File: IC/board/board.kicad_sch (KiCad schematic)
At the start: 35 parts, among them Q1 IRLZ44N, SW1 SW_Push, SW2 SW_Push, SW3 SW_Push, SW4 SW_Push, SW5 SW_Push, SW6 Rotary_Encoder_Switch, U1 L7805, U2 ATmega328P-PU, Y1 16Mhz

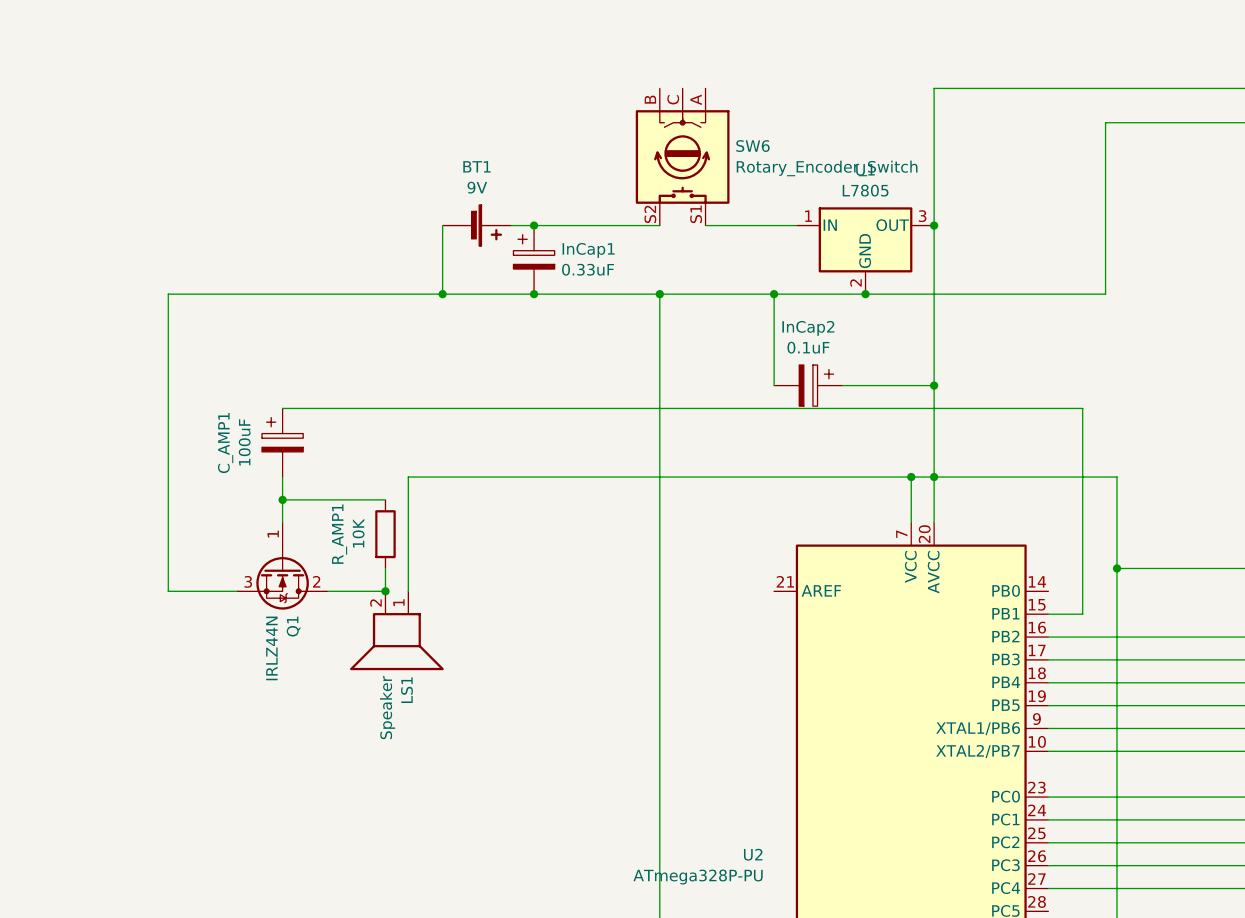
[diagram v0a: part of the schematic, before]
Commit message: Add PAM amplifier
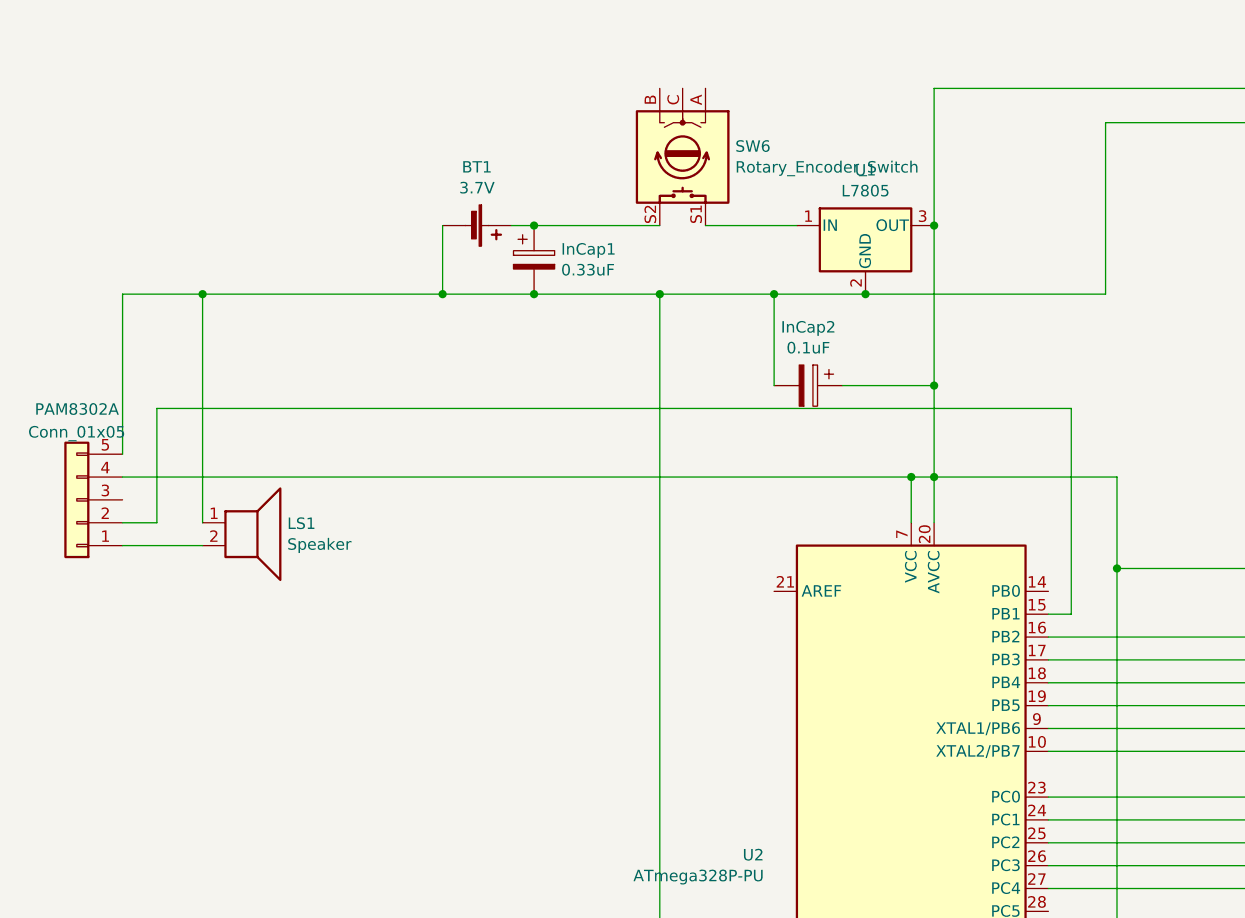
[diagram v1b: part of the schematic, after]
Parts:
- removed C_AMP1: 100uF, Capacitor_THT:CP_Radial_D6.3mm_P2.50mm, symbol Device:CP
- removed Q1: IRLZ44N, Package_TO_SOT_THT:TO-220-3_Vertical, symbol Transistor_FET:IRLZ44N
- removed R_AMP1: 10K, Resistor_THT:R_Axial_DIN0207_L6.3mm_D2.5mm_P7.62mm_Horizontal, symbol Device:R
- added PAM8302A: Conn_01x05, symbol Connector_Generic:Conn_01x05
- BT1: value 9V -> 3.7V
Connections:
- net at InCap2.1, Micro_SD_card1.1 (Pin_1), R_RESET1.2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: now also PAM8302A.4 (Pin_4); no longer LS1.1
- net at BT1.2 (-), C1_CRY1.2, C2_CRY1.2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: now also LS1.1, PAM8302A.5 (Pin_5)
- net at U2.15 (PB1): now also PAM8302A.2 (Pin_2)
- net at LS1.2: now also PAM8302A.1 (Pin_1)
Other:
- moved on the sheet: LS1

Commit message: Remove LED resistors. With new buttons they are not needed
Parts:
- removed R_LED1, R_LED2, R_LED3, R_LED4, R_LED5: 290, Resistor_THT:R_Axial_DIN0207_L6.3mm_D2.5mm_P7.62mm_Horizontal, symbol Device:R
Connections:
- net at U2.23 (PC0): now also LED1.2 (A)
- net at U2.24 (PC1): now also LED2.2 (A)
- net at U2.25 (PC2): now also LED3.2 (A)
- net at U2.26 (PC3): now also LED4.2 (A)
- net at U2.27 (PC4): now also LED5.2 (A)
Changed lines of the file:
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@@
-    (stroke (width 0) (type default) (color 0 0 0 0))
-  )
-  (wire (pts (xy 246.38 67.31) (xy 251.46 67.31))
     (stroke (width 0) (type default) (color 0 0 0 0))
   )
@@
     (stroke (width 0) (type default) (color 0 0 0 0))
   )
-  (wire (pts (xy 241.3 48.26) (xy 251.46 48.26))
-    (stroke (width 0) (type default) (color 0 0 0 0))
-  )
   (wire (pts (xy 123.19 138.43) (xy 123.19 158.75))
     (stroke (width 0) (type default) (color 0 0 0 0))
@@
     (stroke (width 0) (type default) (color 0 0 0 0))
   )
-  (wire (pts (xy 259.08 58.42) (xy 264.16 58.42))
+  (wire (pts (xy 243.84 58.42) (xy 264.16 58.42))
     (stroke (width 0) (type default) (color 0 0 0 0))
   )
@@
     (stroke (width 0) (type default) (color 0 0 0 0))
   )
-  (wire (pts (xy 243.84 58.42) (xy 251.46 58.42))
-    (stroke (width 0) (type default) (color 0 0 0 0))
-  )
   (wire (pts (xy 35.56 64.77) (xy 44.45 64.77))
     (stroke (width 0) (type default) (color 0 0 0 0))
@@
     (stroke (width 0) (type default) (color 0 0 0 0))
   )
-  (wire (pts (xy 259.08 38.1) (xy 264.16 38.1))
+  (wire (pts (xy 238.76 38.1) (xy 264.16 38.1))
     (stroke (width 0) (type default) (color 0 0 0 0))
   )
@@
     (stroke (width 0) (type default) (color 0 0 0 0))
   )
-  (wire (pts (xy 264.16 30.48) (xy 259.08 30.48))
+  (wire (pts (xy 236.22 30.48) (xy 264.16 30.48))
     (stroke (width 0) (type default) (color 0 0 0 0))
   )
@@
     (stroke (width 0) (type default) (color 0 0 0 0))
   )
-  (wire (pts (xy 238.76 38.1) (xy 251.46 38.1))
-    (stroke (width 0) (type default) (color 0 0 0 0))
-  )
   (wire (pts (xy 140.97 49.53) (xy 140.97 72.39))
     (stroke (width 0) (type default) (color 0 0 0 0))
@@
     (stroke (width 0) (type default) (color 0 0 0 0))
   )
-  (wire (pts (xy 236.22 30.48) (xy 251.46 30.48))
-    (stroke (width 0) (type default) (color 0 0 0 0))
-  )
   (wire (pts (xy 162.56 67.31) (xy 146.05 67.31))
     (stroke (width 0) (type default) (color 0 0 0 0))
   )
-  (wire (pts (xy 264.16 67.31) (xy 259.08 67.31))
+  (wire (pts (xy 246.38 67.31) (xy 264.16 67.31))
     (stroke (width 0) (type default) (color 0 0 0 0))
   )
@@
     (stroke (width 0) (type default) (color 0 0 0 0))
   )
-  (wire (pts (xy 264.16 48.26) (xy 259.08 48.26))
+  (wire (pts (xy 241.3 48.26) (xy 264.16 48.26))
     (stroke (width 0) (type default) (color 0 0 0 0))
   )
@@
     (pin "2")
   )
-  (symbol (lib_id "Device:R") (at 255.27 30.48 270) (unit 1)
-    (in_bom yes) (on_board yes)
-    (property "Reference" "R_LED1" (id 0) (at 255.27 25.2222 90))
-    (property "Value" "290" (id 1) (at 255.27 27.5336 90))
-    (property "Footprint" "Resistor_THT:R_Axial_DIN0207_L6.3mm_D2.5mm_P7.62mm_Horizontal" (id 2) (at 255.27 28.702 90)
-      (effects (font (size 1.27 1.27)) hide)
-    )
-    (property "Datasheet" "~" (id 3) (at 255.27 30.48 0)
-      (effects (font (size 1.27 1.27)) hide)
-    )
-    (pin "1")
-    (pin "2")
-  )
-  (symbol (lib_id "Device:R") (at 255.27 38.1 270) (unit 1)
-    (in_bom yes) (on_board yes)
-    (property "Reference" "R_LED2" (id 0) (at 255.27 32.8422 90))
-    (property "Value" "290" (id 1) (at 255.27 35.1536 90))
-    (property "Footprint" "Resistor_THT:R_Axial_DIN0207_L6.3mm_D2.5mm_P7.62mm_Horizontal" (id 2) (at 255.27 36.322 90)
-      (effects (font (size 1.27 1.27)) hide)
-    )
-    (property "Datasheet" "~" (id 3) (at 255.27 38.1 0)
-      (effects (font (size 1.27 1.27)) hide)
-    )
-    (pin "1")
-    (pin "2")
-  )
-  (symbol (lib_id "Device:R") (at 255.27 48.26 270) (unit 1)
-    (in_bom yes) (on_board yes)
-    (property "Reference" "R_LED3" (id 0) (at 255.27 43.0022 90))
-    (property "Value" "290" (id 1) (at 255.27 45.3136 90))
-    (property "Footprint" "Resistor_THT:R_Axial_DIN0207_L6.3mm_D2.5mm_P7.62mm_Horizontal" (id 2) (at 255.27 46.482 90)
-      (effects (font (size 1.27 1.27)) hide)
-    )
-    (property "Datasheet" "~" (id 3) (at 255.27 48.26 0)
-      (effects (font (size 1.27 1.27)) hide)
-    )
-    (pin "1")
-    (pin "2")
-  )
-  (symbol (lib_id "Device:R") (at 255.27 58.42 270) (unit 1)
-    (in_bom yes) (on_board yes)
-    (property "Reference" "R_LED4" (id 0) (at 255.27 53.1622 90))
-    (property "Value" "290" (id 1) (at 255.27 55.4736 90))
-    (property "Footprint" "Resistor_THT:R_Axial_DIN0207_L6.3mm_D2.5mm_P7.62mm_Horizontal" (id 2) (at 255.27 56.642 90)
-      (effects (font (size 1.27 1.27)) hide)
-    )
-    (property "Datasheet" "~" (id 3) (at 255.27 58.42 0)
-      (effects (font (size 1.27 1.27)) hide)
-    )
-    (pin "1")
-    (pin "2")
-  )
-  (symbol (lib_id "Device:R") (at 255.27 67.31 270) (unit 1)
-    (in_bom yes) (on_board yes)
-    (property "Reference" "R_LED5" (id 0) (at 255.27 62.0522 90))
-    (property "Value" "290" (id 1) (at 255.27 64.3636 90))
-    (property "Footprint" "Resistor_THT:R_Axial_DIN0207_L6.3mm_D2.5mm_P7.62mm_Horizontal" (id 2) (at 255.27 65.532 90)
-      (effects (font (size 1.27 1.27)) hide)
-    )
-    (property "Datasheet" "~" (id 3) (at 255.27 67.31 0)
-      (effects (font (size 1.27 1.27)) hide)
-    )
-    (pin "1")
-    (pin "2")
-  )
   (symbol (lib_id "Device:Speaker") (at 49.53 62.23 0) (unit 1)
     (in_bom yes) (on_board yes)
@@
       (reference "PAM8302A") (unit 1) (value "Conn_01x05") (footprint "")
     )
-    (path "/00000000-0000-0000-0000-0000624a90df"
-      (reference "R_LED1") (unit 1) (value "290") (footprint "Resistor_THT:R_Axial_DIN0207_L6.3mm_D2.5mm_P7.62mm_Horizontal")
-    )
-    (path "/00000000-0000-0000-0000-0000624bbc9c"
-      (reference "R_LED2") (unit 1) (value "290") (footprint "Resistor_THT:R_Axial_DIN0207_L6.3mm_D2.5mm_P7.62mm_Horizontal")
-    )
-    (path "/00000000-0000-0000-0000-0000624bdf1c"
-      (reference "R_LED3") (unit 1) (value "290") (footprint "Resistor_THT:R_Axial_DIN0207_L6.3mm_D2.5mm_P7.62mm_Horizontal")
-    )
-    (path "/00000000-0000-0000-0000-0000624c0031"
-      (reference "R_LED4") (unit 1) (value "290") (footprint "Resistor_THT:R_Axial_DIN0207_L6.3mm_D2.5mm_P7.62mm_Horizontal")
-    )
-    (path "/00000000-0000-0000-0000-0000624c1ec2"
-      (reference "R_LED5") (unit 1) (value "290") (footprint "Resistor_THT:R_Axial_DIN0207_L6.3mm_D2.5mm_P7.62mm_Horizontal")
-    )
     (path "/00000000-0000-0000-0000-000062328b24"

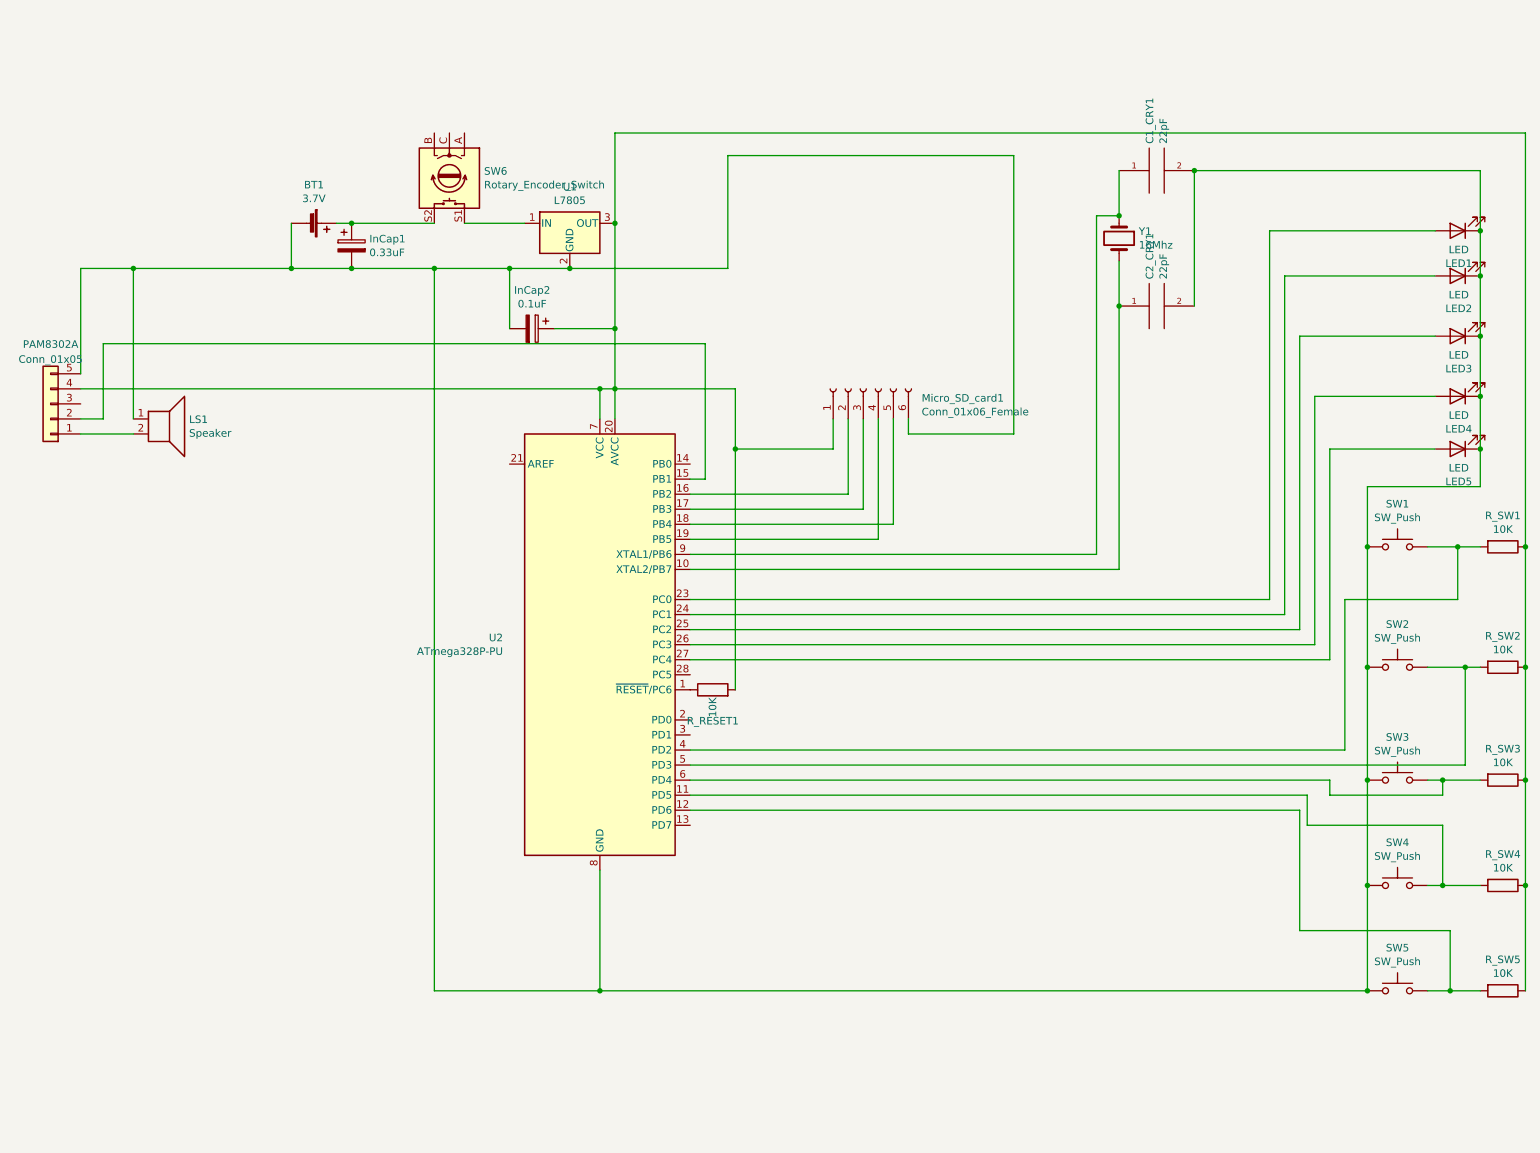
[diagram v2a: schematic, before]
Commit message: Add self power off circuit
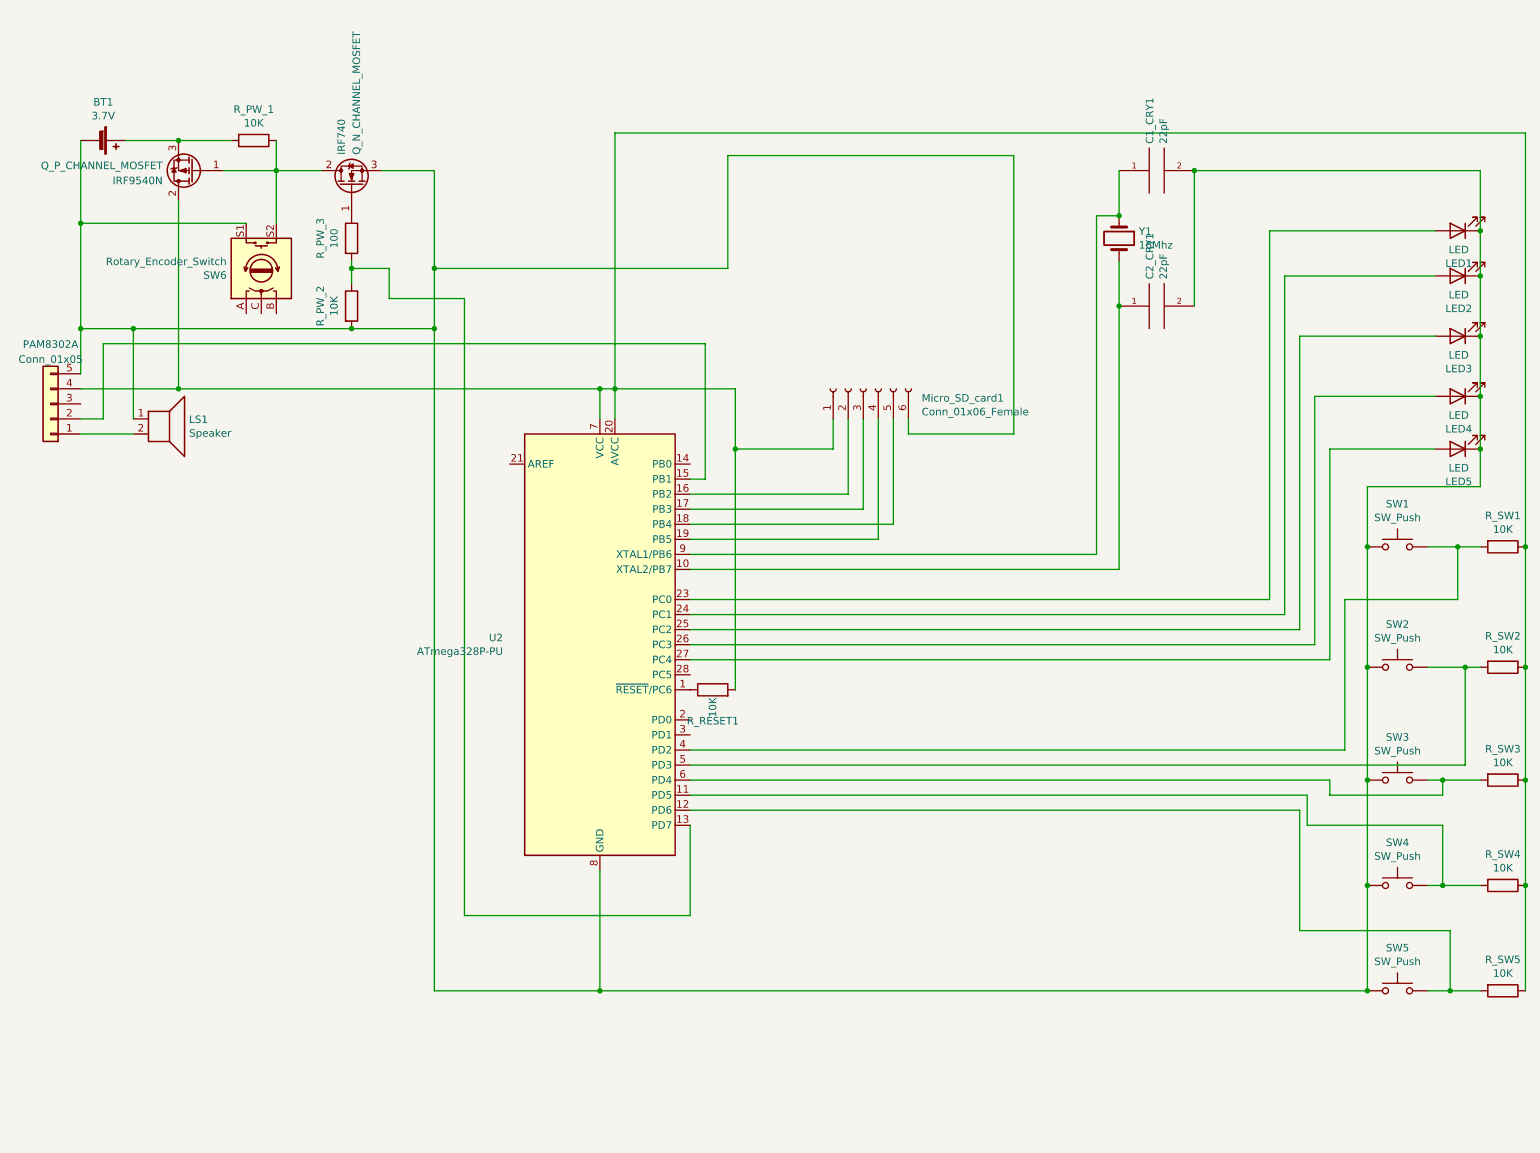
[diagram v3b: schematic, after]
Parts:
- removed InCap1: 0.33uF, Capacitor_THT:CP_Radial_D5.0mm_P2.50mm, symbol Device:CP
- removed InCap2: 0.1uF, Capacitor_THT:CP_Radial_D5.0mm_P2.50mm, symbol Device:CP
- removed U1: L7805, Package_TO_SOT_THT:TO-220-3_Vertical, symbol Regulator_Linear:L7805
- added Q_N_CHANNEL_MOSFET: IRF740, Package_TO_SOT_THT:TO-220-3_Vertical, symbol Transistor_FET:IRF740
- added Q_P_CHANNEL_MOSFET: IRF9540N, Package_TO_SOT_THT:TO-220-3_Vertical, symbol Transistor_FET:IRF9540N
- added R_PW_1, R_PW_2: 10K, Resistor_THT:R_Axial_DIN0207_L6.3mm_D2.5mm_P7.62mm_Horizontal, symbol Device:R
- added R_PW_3: 100, Resistor_THT:R_Axial_DIN0207_L6.3mm_D2.5mm_P7.62mm_Horizontal, symbol Device:R
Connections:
- net at Micro_SD_card1.1 (Pin_1), PAM8302A.4 (Pin_4), R_RESET1.2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: now also Q_P_CHANNEL_MOSFET.2 (D)
- net at BT1.1 (+): now also Q_P_CHANNEL_MOSFET.3 (S), R_PW_1.2; no longer SW6.S2
- net at BT1.2 (-), C1_CRY1.2, C2_CRY1.2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: now also SW6.S1, Q_N_CHANNEL_MOSFET.3 (S), R_PW_2.2
- net at U2.13 (PD7): now also R_PW_2.1, R_PW_3.2
- new net: Q_N_CHANNEL_MOSFET.2 (D), Q_P_CHANNEL_MOSFET.1 (G), R_PW_1.1, SW6.S2
- new net: Q_N_CHANNEL_MOSFET.1 (G), R_PW_3.1
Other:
- moved on the sheet: BT1, SW6
